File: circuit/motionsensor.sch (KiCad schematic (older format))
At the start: 12 parts, among them IC1 ATTINY85-P, K1 CONN_3, P1 CONN_2, P2 CONN_2, Q1 LOCAL_IRF540N, U1 7805

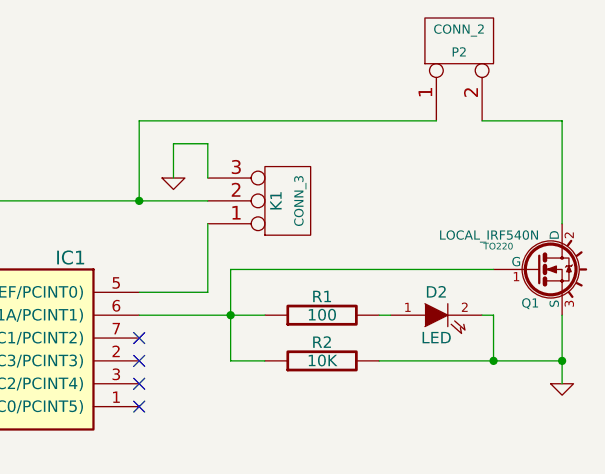
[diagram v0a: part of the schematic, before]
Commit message: Custom IRF540N component wasn't doing anything useful, reverted to stock.
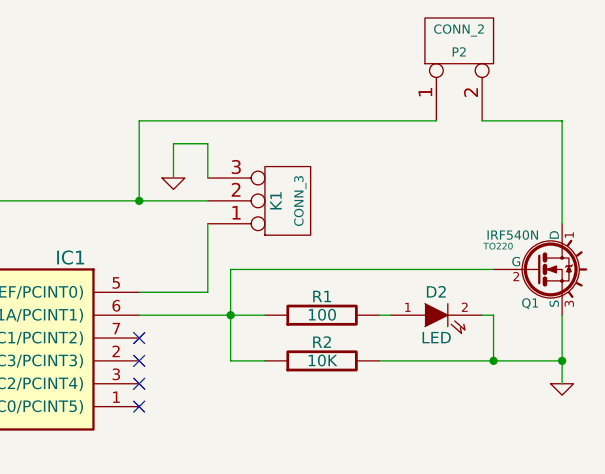
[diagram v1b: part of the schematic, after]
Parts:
- removed Q1: LOCAL_IRF540N, TO220, symbol LOCAL_IRF540N
- added Q1: IRF540N, TO220, symbol IRF540N
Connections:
- net GND: now also Q1.3 (S)
- net at IC1.6 (PB1(MISO/DO/AIN1/OC0B/OC1A/PCINT1)), R1.1, R2.1: now also Q1.2 (G)
- net at P2.2 (PM): now also Q1.1 (D)
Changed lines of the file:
@@
-EESchema Schematic File Version 2  date Tue 02 Jul 2013 14:16:22 EST
+EESchema Schematic File Version 2  date Thu 11 Jul 2013 14:09:32 EST
 LIBS:power
 LIBS:device
@@
 Sheet 1 1
 Title "Motion-activated switch"
-Date "1 jul 2013"
+Date "11 jul 2013"
 Rev "0.2"
 Comp ""
@@
 Comment4 ""
 $EndDescr
-Wire Wire Line
-	8200 3550 9350 3550
+$Comp
+L IRF540N Q1
+U 1 1 51DE2FD3
+P 9550 3550
+F 0 "Q1" H 9550 3402 40  0000 R CNN
+F 1 "IRF540N" H 9550 3699 40  0000 R CNN
+F 2 "TO220" H 9371 3651 29  0000 C CNN
+	1    9550 3550
+	1    0    0    -1
+$EndComp
+Wire Wire Line
+	9350 3550 8200 3550
 Wire Wire Line
 	8200 3550 8200 3950
@@
 	9350 3750 9350 3950
 Connection ~ 9350 3950
-$Comp
-L LOCAL_IRF540N Q1
-U 1 1 51AF5778
-P 9550 3550
-F 0 "Q1" H 9550 3402 40  0000 R CNN
-F 1 "LOCAL_IRF540N" H 9550 3699 40  0000 R CNN
-F 2 "TO220" H 9371 3651 29  0000 C CNN
-	1    9550 3550
-	1    0    0    -1
-$EndComp
 $Comp
 L DIODE D1
@@
 $EndComp
 $Comp
-L GND #PWR5
+L GND #PWR01
 U 1 1 51AE8145
 P 7950 3150
-F 0 "#PWR5" H 7950 3150 30  0001 C CNN
+F 0 "#PWR01" H 7950 3150 30  0001 C CNN
 F 1 "GND" H 7950 3080 30  0001 C CNN
 	1    7950 3150
@@
 $EndComp
 $Comp
-L +12V #PWR3
+L +12V #PWR02
 U 1 1 51A8325B
 P 3150 3150
-F 0 "#PWR3" H 3150 3100 20  0001 C CNN
+F 0 "#PWR02" H 3150 3100 20  0001 C CNN
 F 1 "+12V" H 3150 3250 30  0000 C CNN
 	1    3150 3150
@@
 $EndComp
 $Comp
-L GND #PWR2
+L GND #PWR03
 U 1 1 51A82EEC
 P 2500 3300
-F 0 "#PWR2" H 2500 3300 30  0001 C CNN
+F 0 "#PWR03" H 2500 3300 30  0001 C CNN
 F 1 "GND" H 2500 3230 30  0001 C CNN
 	1    2500 3300
@@
 $EndComp
 $Comp
-L +12V #PWR1
+L +12V #PWR04
 U 1 1 51A82EE5
 P 2250 3250
-F 0 "#PWR1" H 2250 3200 20  0001 C CNN
+F 0 "#PWR04" H 2250 3200 20  0001 C CNN
 F 1 "+12V" H 2250 3350 30  0000 C CNN
 	1    2250 3250
@@
 $EndComp
 $Comp
-L PWR_FLAG #FLG2
+L PWR_FLAG #FLG05
 U 1 1 51A82E5D
 P 2500 3100
-F 0 "#FLG2" H 2500 3195 30  0001 C CNN
+F 0 "#FLG05" H 2500 3195 30  0001 C CNN
 F 1 "PWR_FLAG" H 2500 3280 30  0000 C CNN
 	1    2500 3100
@@
 $EndComp
 $Comp
-L PWR_FLAG #FLG1
+L PWR_FLAG #FLG06
 U 1 1 51A82E58
 P 2250 3100
-F 0 "#FLG1" H 2250 3195 30  0001 C CNN
+F 0 "#FLG06" H 2250 3195 30  0001 C CNN
 F 1 "PWR_FLAG" H 2250 3280 30  0000 C CNN
 	1    2250 3100
@@
 $EndComp
 $Comp
-L GND #PWR7
+L GND #PWR07
 U 1 1 51A829DB
 P 9650 4050
-F 0 "#PWR7" H 9650 4050 30  0001 C CNN
+F 0 "#PWR07" H 9650 4050 30  0001 C CNN
 F 1 "GND" H 9650 3980 30  0001 C CNN
 	1    9650 4050
@@
 $EndComp
 $Comp
-L GND #PWR4
+L GND #PWR08
 U 1 1 51A8185F
 P 3400 4250
-F 0 "#PWR4" H 3400 4250 30  0001 C CNN
+F 0 "#PWR08" H 3400 4250 30  0001 C CNN
 F 1 "GND" H 3400 4180 30  0001 C CNN
 	1    3400 4250
